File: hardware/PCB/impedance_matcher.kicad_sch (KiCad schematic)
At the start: 39 parts, among them Q1 PC817, U1 TLV2372IP

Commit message: Move capacitor closer to op-amp VDD
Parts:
- added FB1: FerriteBead, symbol Device:FerriteBead
- FAN1, OLED1: footprint Connector:B4B-XH-A -> Project Connectors:B4B-XH-A
- I2C1: footprint Connector:B2B-XH-A -> Project Connectors:B2B-XH-A
- SWR1: footprint Connector:B3B-XH-A -> Project Connectors:B3B-XH-A
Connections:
- net GND: now also FB1.2
- net at POWER1.2 (Pin_2), REV_POLARITY1.3: now also FB1.1
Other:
- moved on the sheet: C3, C4, C7, DRIVER1, DRIVER2, MOTOR1, MOTOR2

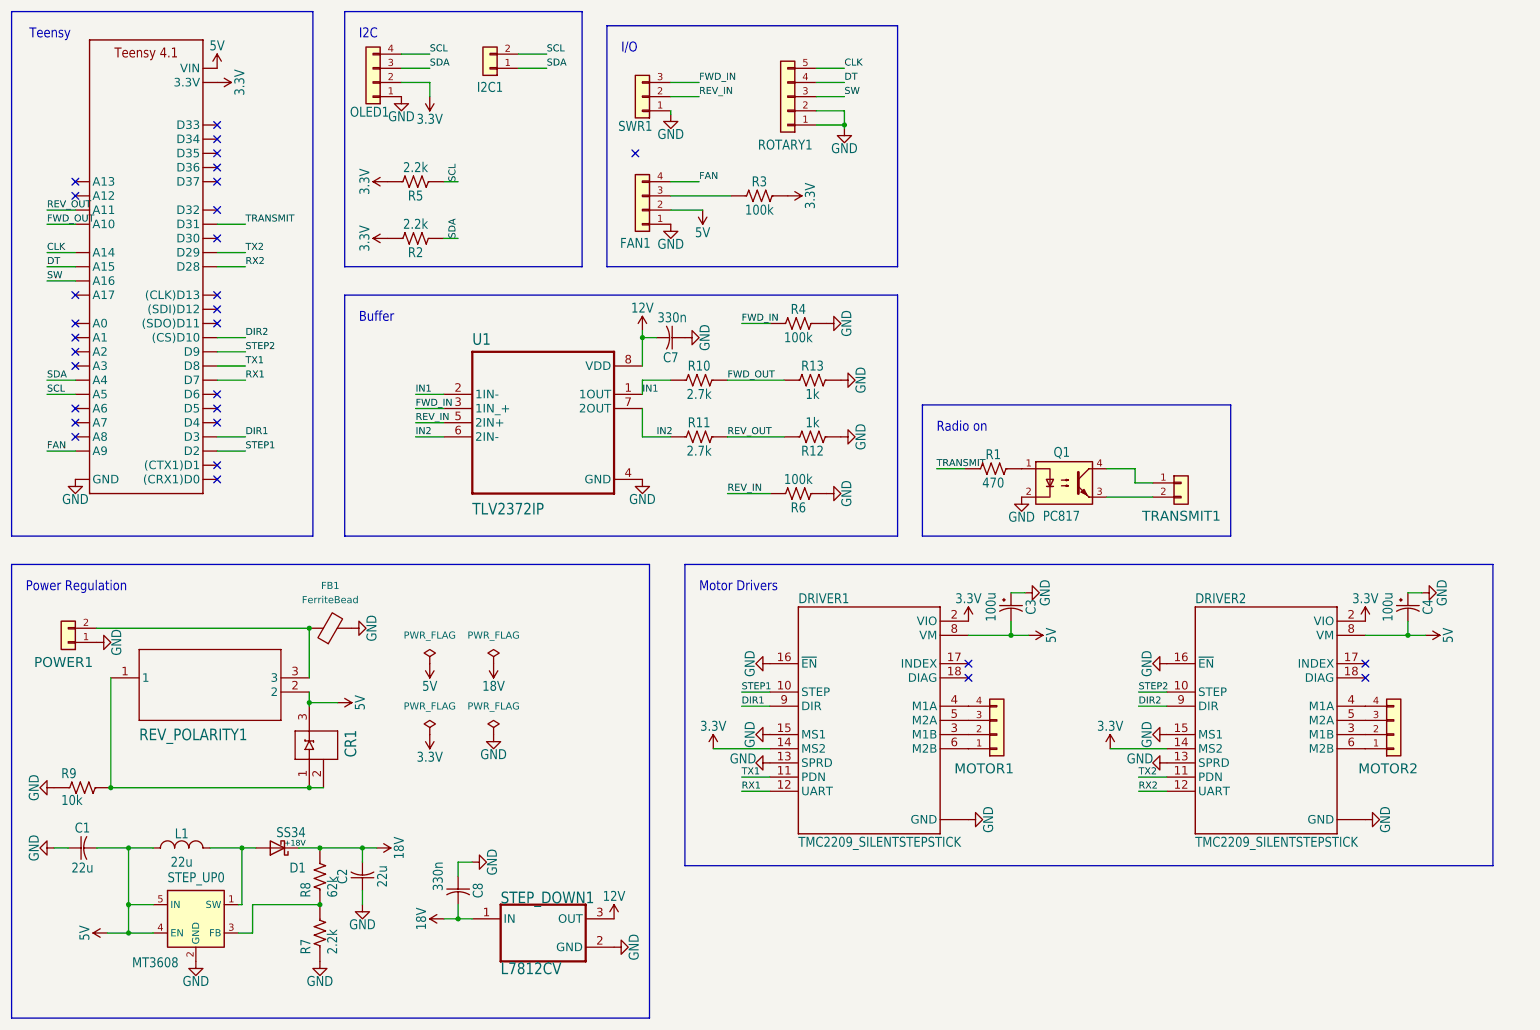
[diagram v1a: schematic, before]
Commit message: Switch to 4 layer PCB and add ferrite beads
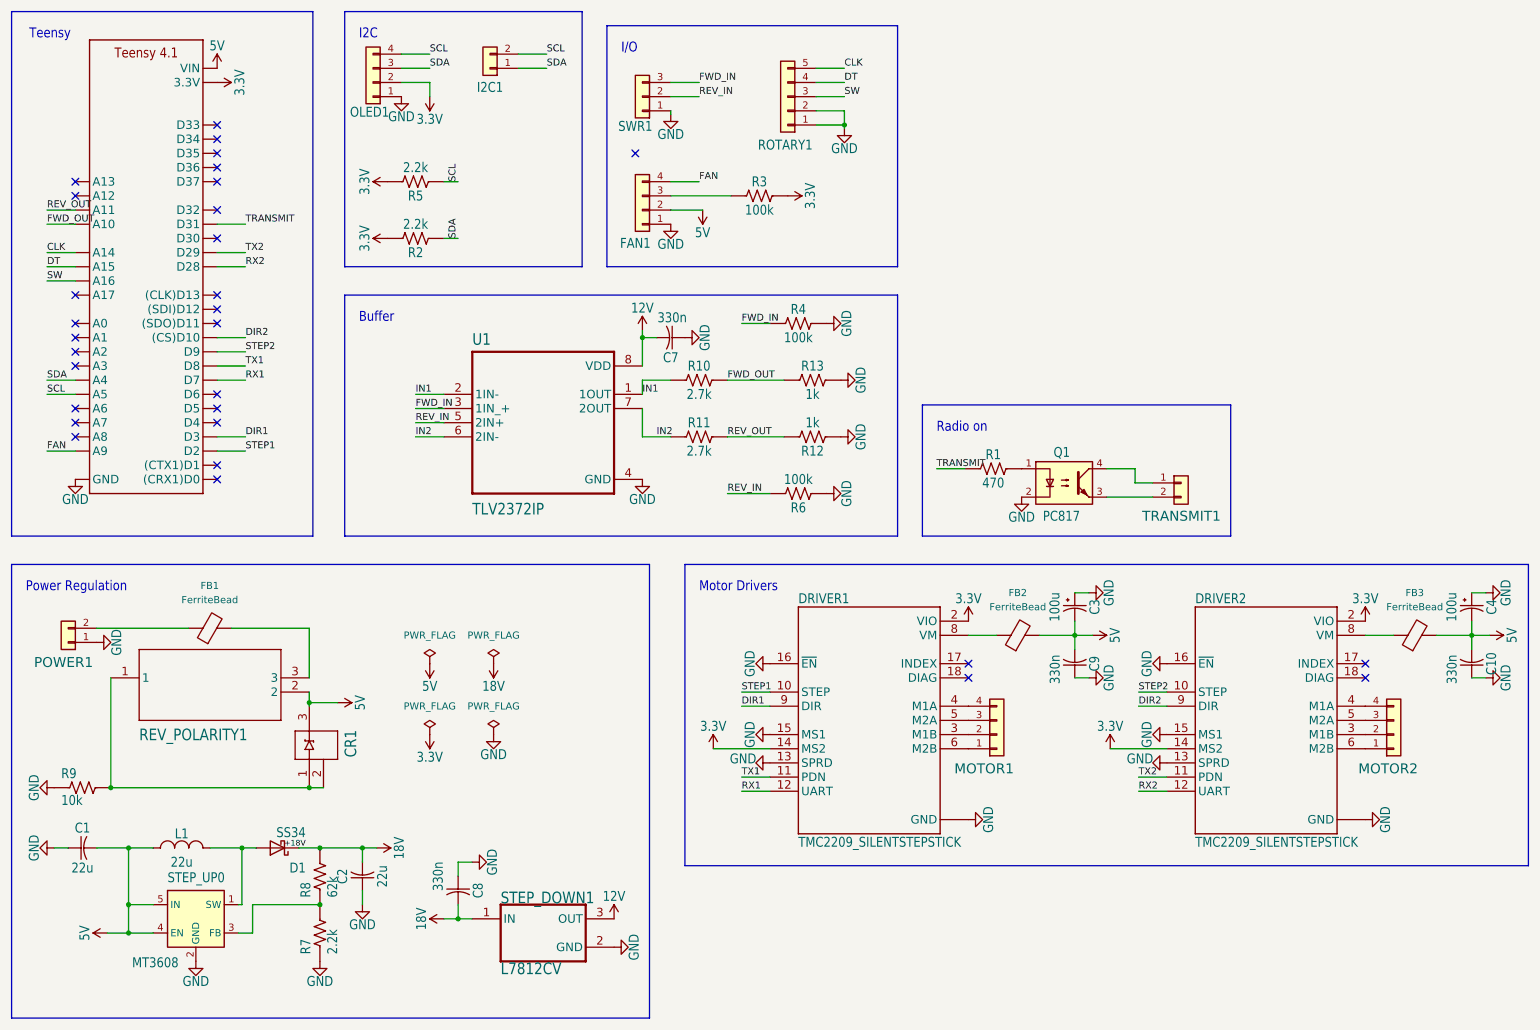
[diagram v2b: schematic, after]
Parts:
- added C10, C9: 330n, Capacitor:CAPC2012X110, symbol Capacitor:C-USCHIP-0805(2012-METRIC)
- added FB2, FB3: FerriteBead, Inductor_SMD:L_0805_2012Metric, symbol Device:FerriteBead
- CR1: value BZX84B24-E3-08SOT-23_2P9X1P3-1P9_VIS -> BZX84C5V6
- FB1: footprint (none) -> Inductor_SMD:L_0805_2012Metric
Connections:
- net 5V: now also C10.2, C9.2, FB2.2, FB3.2; no longer DRIVER1.8 (VM), DRIVER2.8 (VM)
- net GND: now also C10.1, C9.1; no longer FB1.2
- net at FB1.1, POWER1.2 (Pin_2): no longer REV_POLARITY1.3
- new net: FB1.2, REV_POLARITY1.3
- new net: DRIVER1.8 (VM), FB2.1
- new net: DRIVER2.8 (VM), FB3.1
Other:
- moved on the sheet: C3, C4, FB1

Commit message: Switch all resistors to 0805
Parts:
- C1, C2: LCSC Part (none) -> C45783
- C10, C7, C8, C9: LCSC Part (none) -> C1740
- CR1: LCSC Part (none) -> C148101
- D1: LCSC Part (none) -> C8678
- FB1, FB2, FB3: LCSC Part (none) -> C15957
- L1: LCSC Part (none) -> C9391
- Q1: LCSC Part (none) -> C20612593
- R1: LCSC Part (none) -> C17710
- R10, R11: footprint Resistor:RESC3216X70 -> Resistor:RESC2012X65; LCSC Part (none) -> C17530
- R12, R13: footprint Resistor:RESC3216X70 -> Resistor:RESC2012X65; LCSC Part (none) -> C17513
- R2, R5: footprint Resistor:RESC3216X70 -> Resistor:RESC2012X65; LCSC Part (none) -> C17520
- R3: LCSC Part (none) -> C149504
- R4, R6: footprint Resistor:RESC3216X70 -> Resistor:RESC2012X65; LCSC Part (none) -> C149504
- R7: LCSC Part (none) -> C17520
- R8: LCSC Part (none) -> C17783
- R9: LCSC Part (none) -> C17414
- REV_POLARITY1: LCSC Part (none) -> C93034
- STEP_DOWN1: LCSC Part (none) -> C105651
- STEP_UP0: LCSC Part (none) -> C84817
